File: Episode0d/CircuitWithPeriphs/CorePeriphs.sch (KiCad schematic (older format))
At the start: 6 parts, among them U301 82C55A, U302 82C54, U303 MC6850

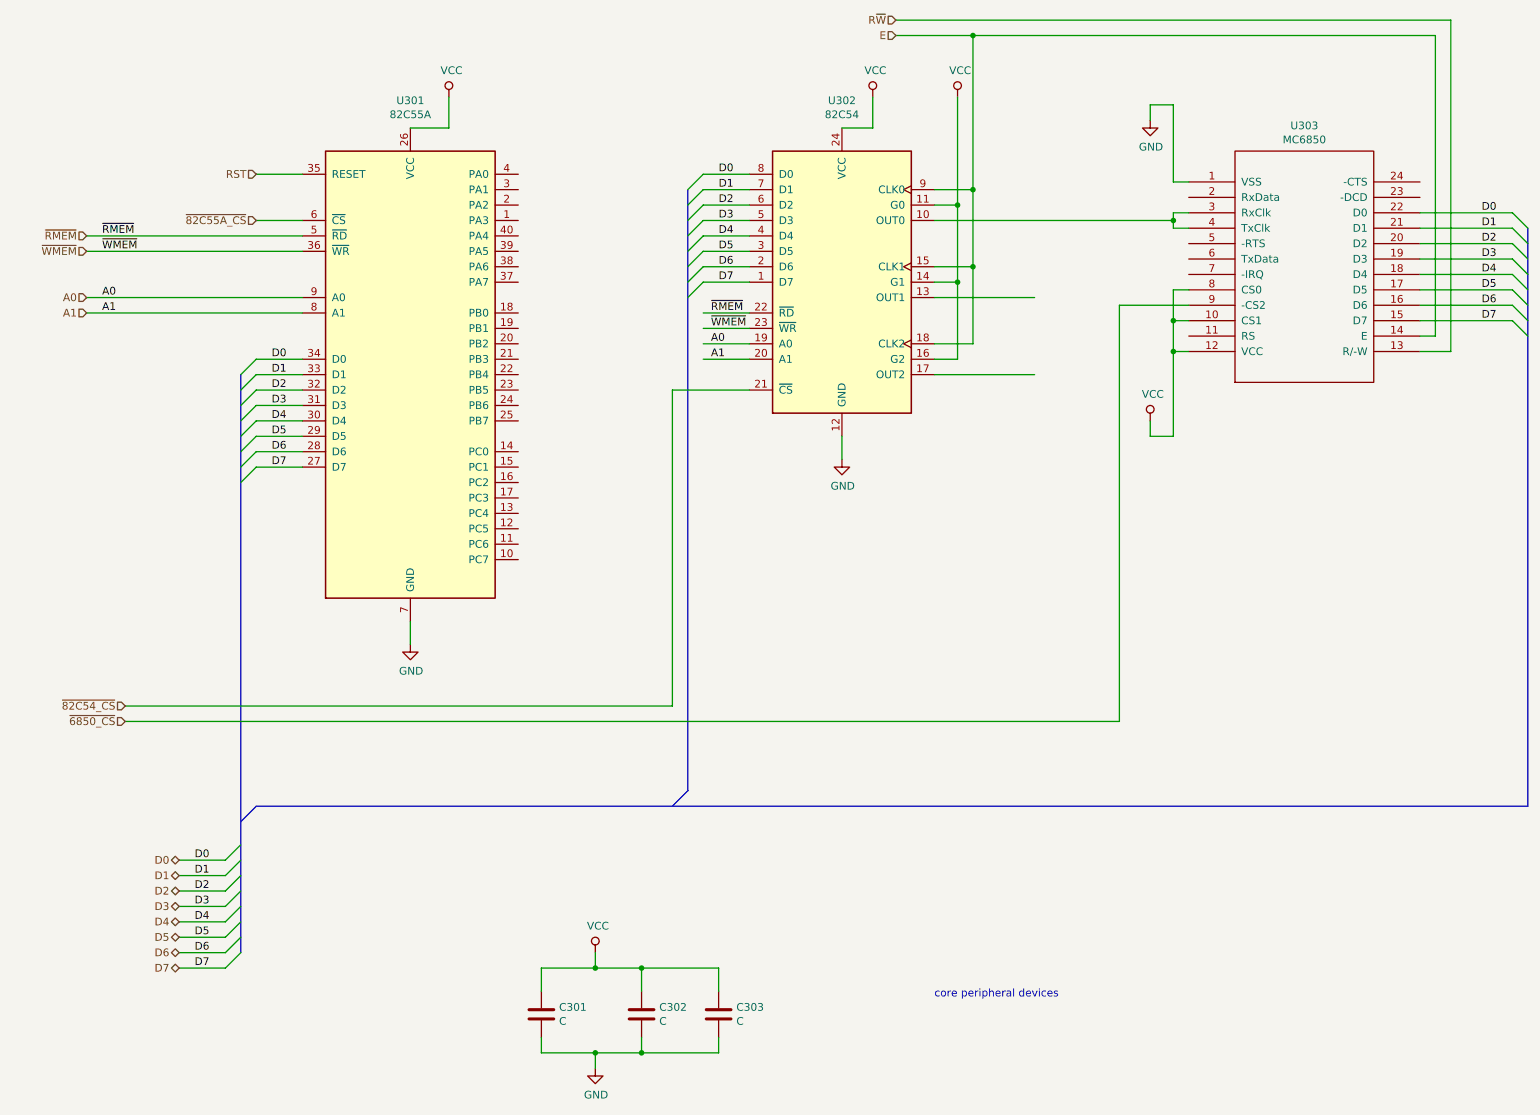
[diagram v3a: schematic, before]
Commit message: show ACIA connections to FT232RL breakout
Use current-limiting resistors between ACIA and FT232RL,
since they are powered by different sources, and we don't
want current flow between them.  (Got this idea from
Grant Searle's minimal 6809 project.)  Not sure if the
FT232RL should have its VCC connected to the 6809 system's
VCC: need to check old prototype.
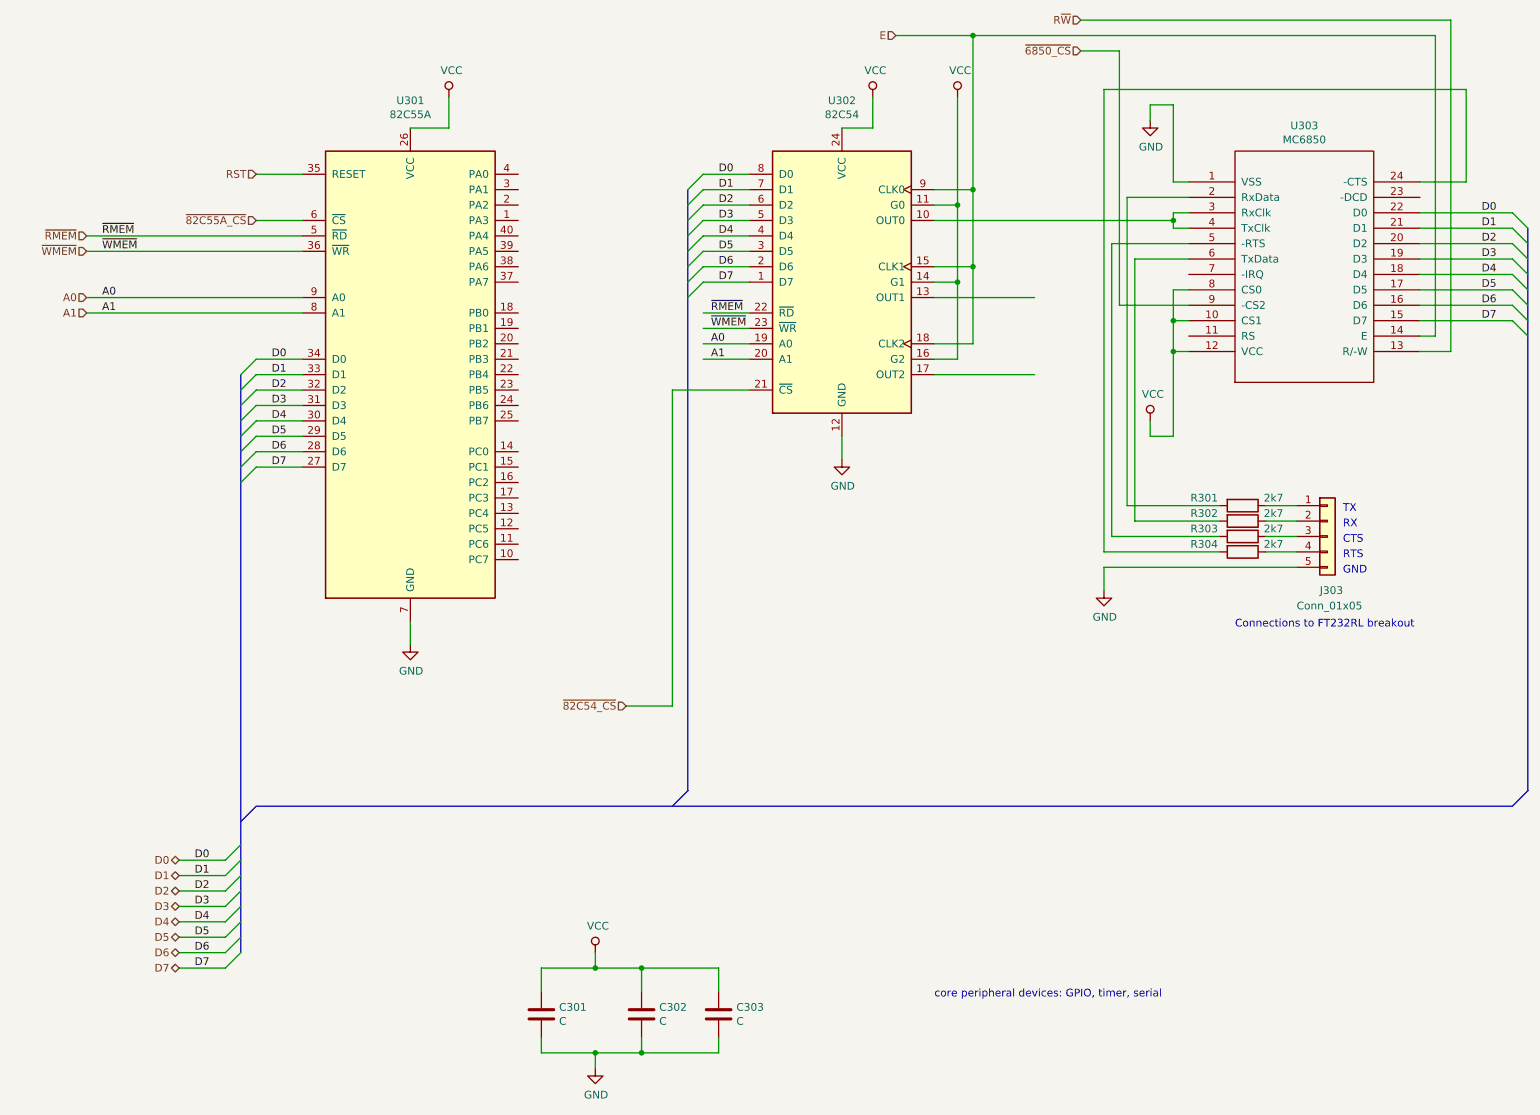
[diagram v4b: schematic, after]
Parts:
- added J303: Conn_01x05, symbol Connector_Generic:Conn_01x05
- added R301, R302, R303, R304: 2k7, symbol device:R
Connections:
- wire segments 106 -> 126
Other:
- note added: "CTS"
- note added: "Connections to FT232RL breakout"
- note added: "GND"
- note added: "RTS"
- note added: "RX"
- note added: "TX"
- note added: "core peripheral devices: GPIO, timer, serial"
- note removed: "core peripheral devices"
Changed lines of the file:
@@
 $EndComp
 Text Notes 6350 6950 0    50   ~ 0
-core peripheral devices
+core peripheral devices: GPIO, timer, serial
 Wire Wire Line
 	2950 1300 3200 1300
@@
 	1    0    0    -1
 $EndComp
-Text HLabel 1100 5050 0    50   Input ~ 0
+Text HLabel 4350 5050 0    50   Input ~ 0
 ~82C54_CS
 Wire Wire Line
@@
 	4650 3000 4650 5050
 Wire Wire Line
-	4650 5050 1100 5050
+	4650 5050 4350 5050
 Wire Wire Line
 	5750 3300 5750 3450
@@
 	9600 700  6600 700
 Connection ~ 6600 700
-Text HLabel 6100 600  0    50   Input ~ 0
+Text HLabel 7300 600  0    50   Input ~ 0
 R~W
 Wire Wire Line
@@
 	9700 2750 9700 600
 Wire Wire Line
-	9700 600  6100 600
+	9700 600  7300 600
 Wire Wire Line
 	7900 1900 7900 1850
@@
 	7900 1950 7900 1900
 Connection ~ 7900 1900
-Text HLabel 1100 5150 0    50   Input ~ 0
+Text HLabel 7300 800  0    50   Input ~ 0
 ~6850_CS
 Wire Wire Line
-	1100 5150 7550 5150
-Wire Wire Line
-	7550 5150 7550 2450
+	7300 800  7550 800
+Wire Wire Line
+	7550 800  7550 2450
 Wire Wire Line
 	7550 2450 8000 2450
@@
 Wire Wire Line
 	4950 7300 4450 7300
+Connection ~ 4450 7300
+Entry Bus Bus
+	10100 5700 10200 5600
+$Comp
+L Connector_Generic:Conn_01x05 J303
+U 1 1 5DE6A143
+P 8900 3950
+F 0 "J303" H 8850 3600 50  0000 L CNN
+F 1 "Conn_01x05" H 8700 3500 50  0000 L CNN
+F 2 "" H 8900 3950 50  0001 C CNN
+F 3 "~" H 8900 3950 50  0001 C CNN
+	1    8900 3950
+	1    0    0    -1
+$EndComp
+Text Notes 8300 4550 0    50   ~ 0
+Connections to FT232RL breakout
+Text Notes 9000 3800 0    50   ~ 0
+TX
+Text Notes 9000 3900 0    50   ~ 0
+RX
+Text Notes 9000 4000 0    50   ~ 0
+CTS
+Text Notes 9000 4100 0    50   ~ 0
+RTS
+Text Notes 9000 4200 0    50   ~ 0
+GND
+Wire Wire Line
+	8000 1750 7600 1750
+Wire Wire Line
+	7600 1750 7600 3750
+Wire Wire Line
+	8000 2150 7650 2150
+Wire Wire Line
+	7650 2150 7650 3850
+Wire Wire Line
+	8000 2050 7500 2050
+Wire Wire Line
+	7500 2050 7500 3950
+Wire Wire Line
+	9500 1650 9800 1650
+Wire Wire Line
+	9800 1650 9800 1050
+Wire Wire Line
+	9800 1050 7450 1050
+Wire Wire Line
+	7450 1050 7450 4050
+Wire Wire Line
+	7450 4150 7450 4300
+$Comp
+L power:GND #PWR?
+U 1 1 5DE7EF8C
+P 7450 4300
+F 0 "#PWR?" H 7450 4050 50  0001 C CNN
+F 1 "GND" H 7455 4127 50  0000 C CNN
+F 2 "" H 7450 4300 50  0001 C CNN
+F 3 "" H 7450 4300 50  0001 C CNN
+	1    7450 4300
+	1    0    0    -1
+$EndComp
+Wire Wire Line
+	7450 4150 8700 4150
+$Comp
+L device:R R301
+U 1 1 5DE91934
+P 8350 3750
+F 0 "R301" V 8300 3500 50  0000 C CNN
+F 1 "2k7" V 8300 3950 50  0000 C CNN
+F 2 "" V 8280 3750 50  0001 C CNN
+F 3 "" H 8350 3750 50  0001 C CNN
+	1    8350 3750
+	0    1    1    0
+$EndComp
+$Comp
+L device:R R302
+U 1 1 5DE954B6
+P 8350 3850
+F 0 "R302" V 8300 3600 50  0000 C CNN
+F 1 "2k7" V 8300 4050 50  0000 C CNN
+F 2 "" V 8280 3850 50  0001 C CNN
+F 3 "" H 8350 3850 50  0001 C CNN
+	1    8350 3850
+	0    1    1    0
+$EndComp
+$Comp
+L device:R R303
+U 1 1 5DE98E9C
+P 8350 3950
+F 0 "R303" V 8300 3700 50  0000 C CNN
+F 1 "2k7" V 8300 4150 50  0000 C CNN
+F 2 "" V 8280 3950 50  0001 C CNN
+F 3 "" H 8350 3950 50  0001 C CNN
+	1    8350 3950
+	0    1    1    0
+$EndComp
+$Comp
+L device:R R304
+U 1 1 5DE98EA2
+P 8350 4050
+F 0 "R304" V 8300 3800 50  0000 C CNN
+F 1 "2k7" V 8300 4250 50  0000 C CNN
+F 2 "" V 8280 4050 50  0001 C CNN
+F 3 "" H 8350 4050 50  0001 C CNN
+	1    8350 4050
+	0    1    1    0
+$EndComp
+Wire Wire Line
+	7600 3750 8200 3750
+Wire Wire Line
+	7650 3850 8200 3850
+Wire Wire Line
+	7500 3950 8200 3950
+Wire Wire Line
+	7450 4050 8200 4050
+Wire Wire Line
+	8500 3750 8700 3750
+Wire Wire Line
+	8500 3850 8700 3850
+Wire Wire Line
+	8500 3950 8700 3950
+Wire Wire Line
+	8500 4050 8700 4050
 Wire Bus Line
-	1950 5700 10200 5700
-Wire Bus Line
-	10200 1950 10200 5700
+	1950 5700 10100 5700
 Wire Bus Line
 	4750 1700 4750 5600
 Wire Bus Line
+	10200 1950 10200 5600
+Wire Bus Line
 	1850 2900 1850 6650
-Connection ~ 4450 7300
 $EndSCHEMATC

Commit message: still trying to get ACIA working
Forgot to route A0 to the RS input on the ACIA,
fixed, hopefully it will work now.
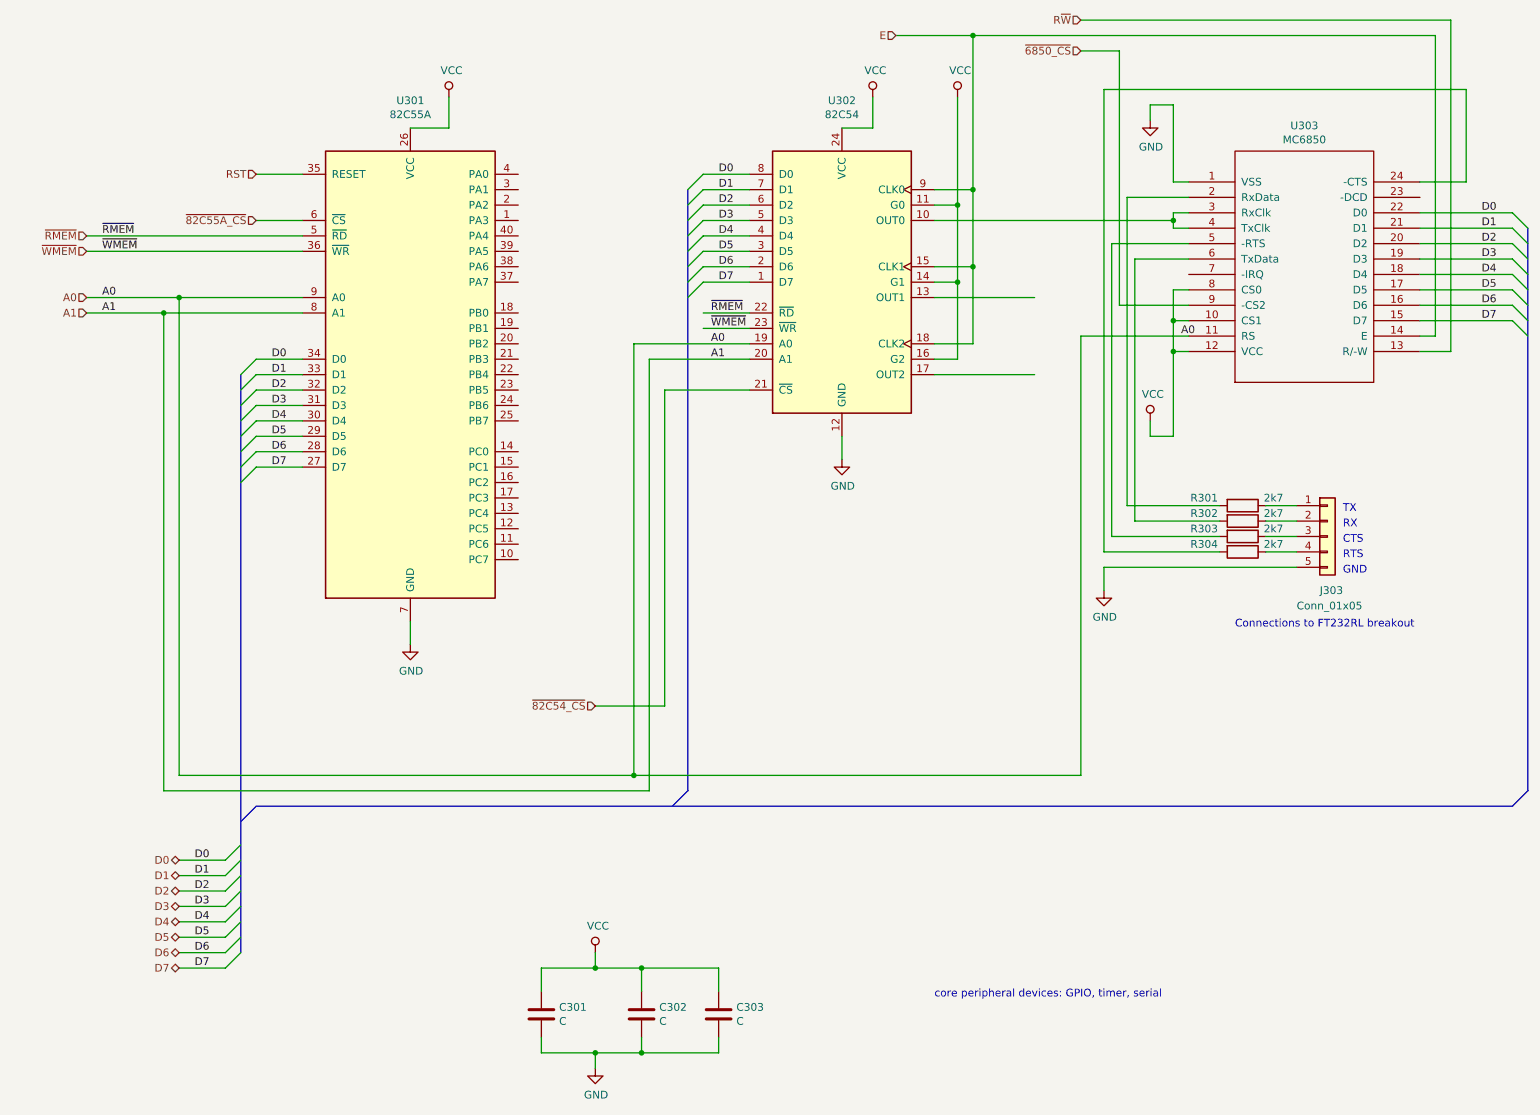
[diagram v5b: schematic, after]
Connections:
- wire segments 126 -> 137
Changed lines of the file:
@@
 $EndComp
 Wire Wire Line
-	2250 2400 850  2400
-Wire Wire Line
-	2250 2500 850  2500
+	2250 2400 1450 2400
+Wire Wire Line
+	2250 2500 1350 2500
 Wire Wire Line
 	2250 1900 1950 1900
@@
 Text Label 950  2500 0    50   ~ 0
 A1
-Wire Wire Line
-	5150 2700 4850 2700
-Wire Wire Line
-	5150 2800 4850 2800
 Text Label 4900 2700 0    50   ~ 0
 A0
@@
 	1    0    0    -1
 $EndComp
-Text HLabel 4350 5050 0    50   Input ~ 0
+Text HLabel 4150 5050 0    50   Input ~ 0
 ~82C54_CS
 Wire Wire Line
-	5150 3000 4650 3000
-Wire Wire Line
-	4650 3000 4650 5050
-Wire Wire Line
-	4650 5050 4350 5050
+	5150 3000 4600 3000
+Wire Wire Line
+	4600 3000 4600 5050
+Wire Wire Line
+	4600 5050 4150 5050
 Wire Wire Line
 	5750 3300 5750 3450
@@
 Wire Wire Line
 	8500 4050 8700 4050
+Text Label 7950 2650 0    50   ~ 0
+A0
+Wire Wire Line
+	4400 2700 4400 5500
+Wire Wire Line
+	4400 5500 1450 5500
+Wire Wire Line
+	1450 5500 1450 2400
+Wire Wire Line
+	4400 2700 5150 2700
+Connection ~ 1450 2400
+Wire Wire Line
+	1450 2400 850  2400
+Wire Wire Line
+	4500 2800 4500 5600
+Wire Wire Line
+	4500 5600 1350 5600
+Wire Wire Line
+	1350 5600 1350 2500
+Wire Wire Line
+	4500 2800 5150 2800
+Connection ~ 1350 2500
+Wire Wire Line
+	1350 2500 850  2500
+Wire Wire Line
+	7300 2650 7300 5500
+Wire Wire Line
+	7300 5500 4400 5500
+Wire Wire Line
+	7300 2650 8000 2650
 Wire Bus Line
 	1950 5700 10100 5700
@@
 Wire Bus Line
 	1850 2900 1850 6650
+Connection ~ 4400 5500
 $EndSCHEMATC

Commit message: make a note about 6850/FT232RL conns being wrong
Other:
- note added: "THIS SCHEMATIC IS WRONG!\nSee the schematic in Episode0f\nfor correct way to interface\n6850 ACIA and FT232RL breakout"
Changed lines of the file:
@@
 Wire Wire Line
 	7300 2650 8000 2650
+Connection ~ 4400 5500
 Wire Bus Line
 	1950 5700 10100 5700
@@
 Wire Bus Line
 	1850 2900 1850 6650
-Connection ~ 4400 5500
+Text Notes 8200 3450 0    50   ~ 0
+THIS SCHEMATIC IS WRONG!\nSee the schematic in Episode0f\nfor correct way to interface\n6850 ACIA and FT232RL breakout
 $EndSCHEMATC
